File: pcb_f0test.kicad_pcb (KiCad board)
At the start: 2 copper layers, 50 x 50 mm, 93 parts, among them P1 CONN_02X05, P2 CONN_01X02, P3 CONN_01X06, P5 CONN_02X05, P6 CONN_02X05, P7 CONN_01X01, P8 CONN_01X01, U1 STM32F042GxU, U2 LP2985LV, U3 KNUSB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

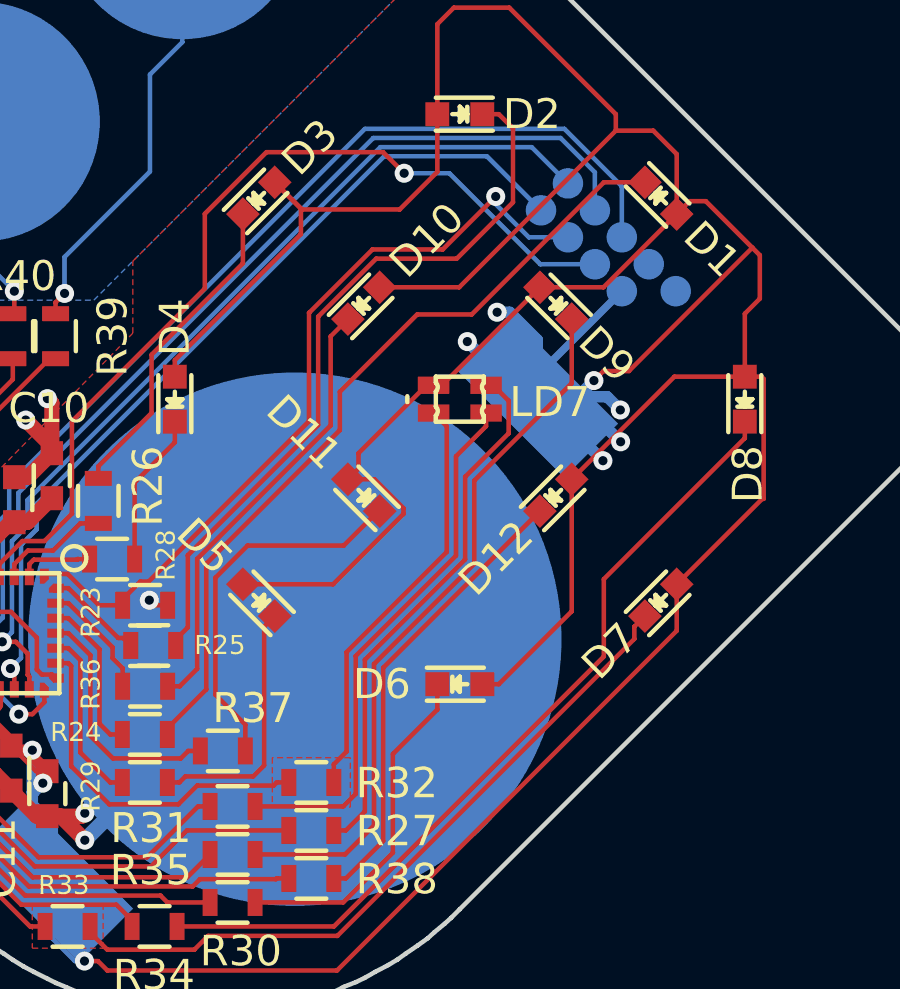
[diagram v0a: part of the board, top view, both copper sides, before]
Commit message: Switch RGB LED on heart PCB to new type/pinout.
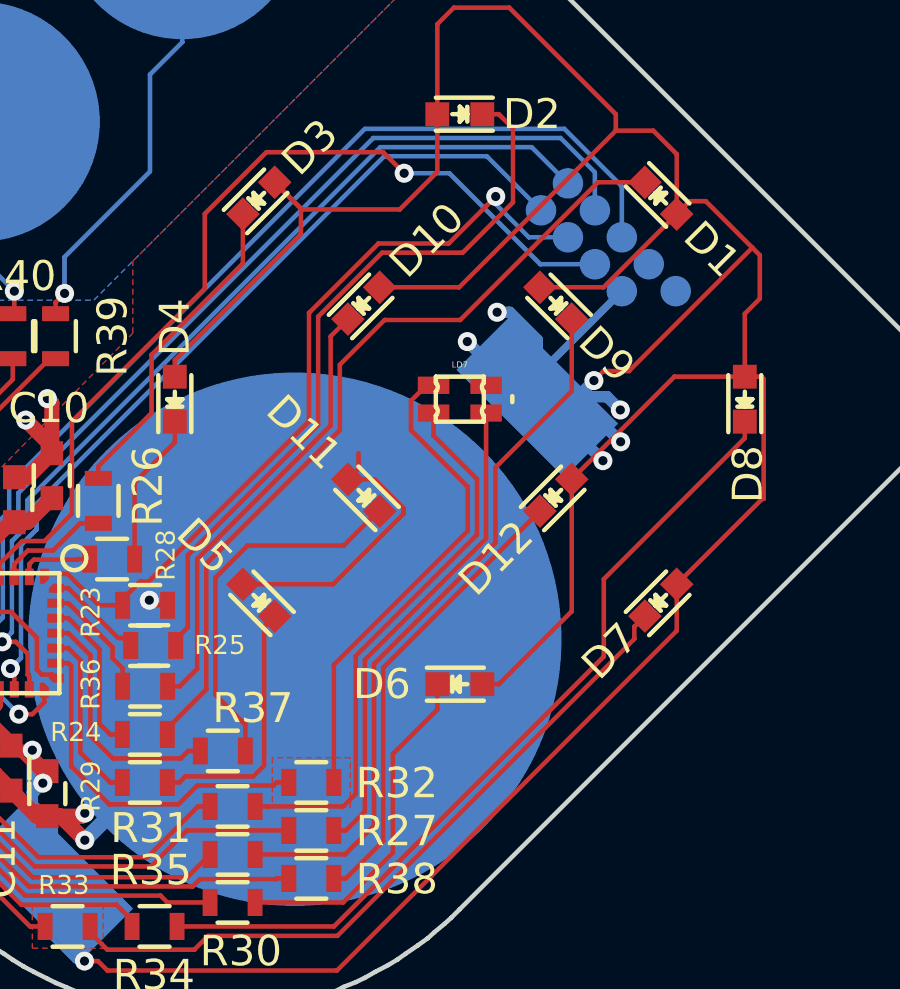
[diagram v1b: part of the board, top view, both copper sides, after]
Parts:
- LD7: footprint knielsenlib:RGB_0603 -> knielsenlib:RGB_0603_ALTPINOUT
- turned LD7 to 0 degrees
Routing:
- net +2V5: track 180.3 -> 172.0 mm
- net /sheet_heart/h_ildb1: track 14.1 -> 16.3 mm
- net /sheet_heart/h_ildr1: track 17.9 -> 16.3 mm
- net /sheet_heart/h_ild1: track 26.9 -> 27.4 mm

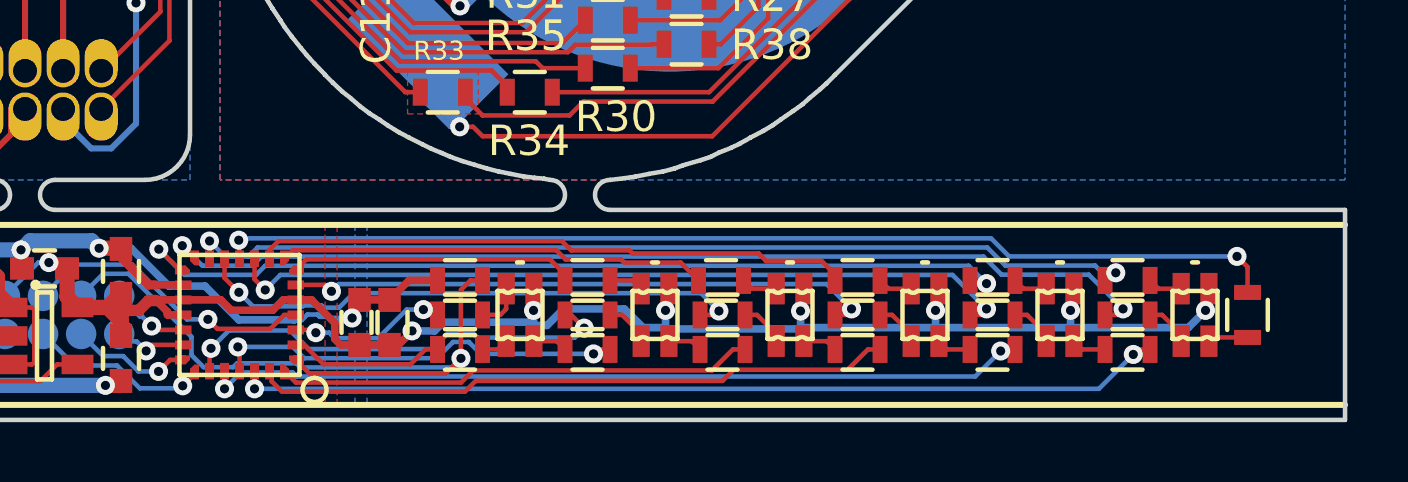
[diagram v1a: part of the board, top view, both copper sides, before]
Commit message: Change RGB LED footprint to match new batch of cheap 0603.
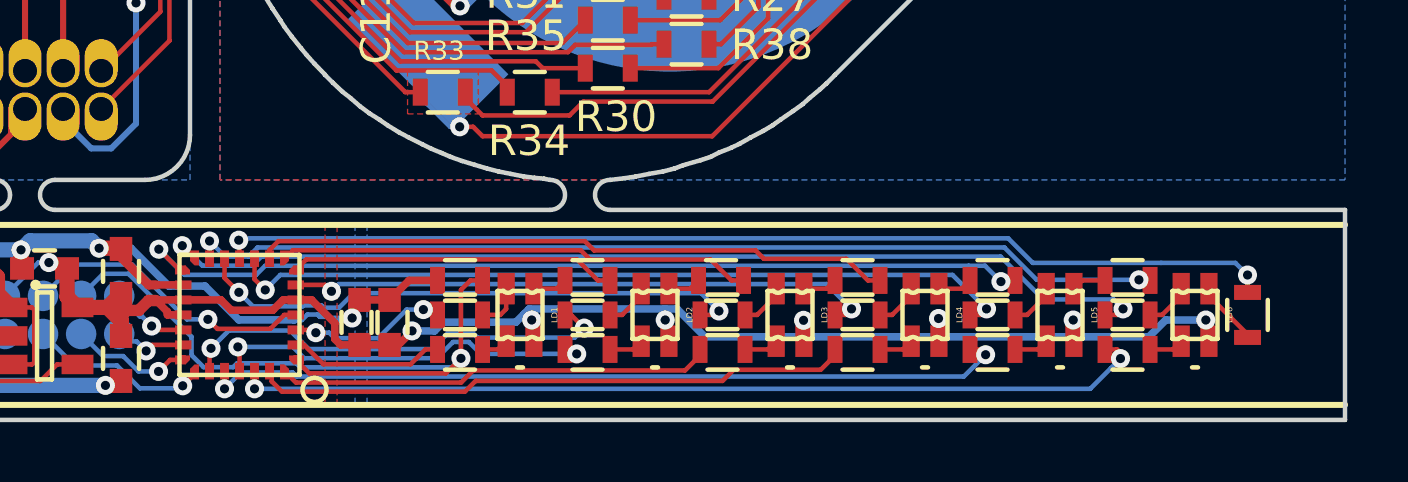
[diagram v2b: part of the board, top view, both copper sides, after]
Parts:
- LD1, LD2, LD3, LD4, LD5, LD6: footprint knielsenlib:RGB_0603 -> knielsenlib:RGB_0603_ALTPINOUT
- R2: value 560 -> 100
- R5: value 100 -> 560
- turned LD1 to 270 degrees
- turned LD2 to 270 degrees
- turned LD3 to 270 degrees
- turned LD4 to 270 degrees
- turned LD5 to 270 degrees
- turned LD6 to 270 degrees
- turned R12 to 180 degrees
- turned R13 to 180 degrees
- turned R14 to 0 degrees
- turned R15 to 0 degrees
- turned R18 to 180 degrees
- turned R19 to 180 degrees
- turned R3 to 0 degrees
- turned R6 to 180 degrees
- turned R8 to 0 degrees
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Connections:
- LD1 pad 2: /ildr2 -> /ildr1
- LD1 pad 3: /ildg2 -> /ildg1
- LD1 pad 4: /ildb2 -> /ildb1
- LD2 pad 2: /ildr3 -> /ildr2
- LD2 pad 3: /ildg3 -> /ildg2
- LD2 pad 4: /ildb3 -> /ildb2
- LD3 pad 2: /ildr4 -> /ildr3
- LD3 pad 3: /ildg4 -> /ildg3
- LD3 pad 4: /ildb4 -> /ildb3
- LD4 pad 2: /ildr5 -> /ildr4
- LD4 pad 3: /ildg5 -> /ildg4
- LD4 pad 4: /ildb5 -> /ildb4
- LD5 pad 2: /ildr6 -> /ildr5
- LD5 pad 3: /ildg6 -> /ildg5
- LD5 pad 4: /ildb6 -> /ildb5
- LD6 pad 2: /ildr1 -> /ildr6
- LD6 pad 3: /ildg1 -> /ildg6
- LD6 pad 4: /ildb1 -> /ildb6
- R10 pad 1: /ldg3 -> /ldg2
- R10 pad 2: /ildg3 -> /ildg2
- R11 pad 1: /ldg4 -> /ldg3
- R11 pad 2: /ildg4 -> /ildg3
- R12 pad 1: /ldb3 -> /ldb1
- R12 pad 2: /ildb3 -> /ildb1
- R13 pad 1: /ldb4 -> /ldb2
- R13 pad 2: /ildb4 -> /ildb2
- R16 pad 1: /ldg5 -> /ldg4
- R16 pad 2: /ildg5 -> /ildg4
- R17 pad 1: /ldg6 -> /ldg5
- R17 pad 2: /ildg6 -> /ildg5
- R18 pad 1: /ldb5 -> /ldb3
- R18 pad 2: /ildb5 -> /ildb3
- R19 pad 1: /ldb6 -> /ldb4
- R19 pad 2: /ildb6 -> /ildb4
- R2 pad 1: /ldr1 -> /ldb6
- R2 pad 2: /ildr1 -> /ildb6
- R4 pad 1: /ldg1 -> /ldg6
- R4 pad 2: /ildg1 -> /ildg6
- R5 pad 1: /ldg2 -> /ldr1
- R5 pad 2: /ildg2 -> /ildr1
- R6 pad 1: /ldb1 -> /ldb5
- R6 pad 2: /ildb1 -> /ildb5
- R7 pad 1: /ldb2 -> /ldg1
- R7 pad 2: /ildb2 -> /ildg1
- U1 pad 10: /ldg6 -> /ldg5
- U1 pad 11: /ldr1 -> /ldb6
- U1 pad 12: /ldg4 -> /ldg3
- U1 pad 13: /ldb1 -> /ldb5
- U1 pad 14: /ldg1 -> /ldg6
- U1 pad 15: /ldb6 -> /ldb4
- U1 pad 2: /ldg2 -> /ldr1
- U1 pad 23: /ldg3 -> /ldg2
- U1 pad 3: /ldb2 -> /ldg1
- U1 pad 6: /ldg5 -> /ldg4
- U1 pad 7: /ldb3 -> /ldb1
- U1 pad 8: /ldb4 -> /ldb2
- U1 pad 9: /ldb5 -> /ldb3
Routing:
- net /ldr1: track 35.5 -> 5.20 mm, vias 2 -> 0
- net /ldg1: track 33.8 -> 5.37 mm
- net /ldb1: track 32.0 -> 10.9 mm, vias 2 -> 0
- net /ldb4: track 14.3 -> 30.4 mm, vias 0 -> 2
- net /ldb5: track 19.9 -> 32.7 mm, vias 0 -> 2
- net /ldb3: track 9.53 -> 21.3 mm
- net /ldb2: track 5.37 -> 15.8 mm, vias 2 -> 0
- net /ldg2: track 5.20 -> 15.0 mm, vias 0 -> 2
- net /ldg6: track 26.5 -> 33.8 mm
- net /ldg5: track 19.7 -> 26.5 mm
- net /ldb6: track 30.2 -> 35.4 mm
- net /ldg3: track 15.0 -> 18.7 mm
- net /ldr3: track 16.0 -> 14.6 mm
- net /ldr4: track 21.4 -> 20.0 mm
- net /ildb6: track 1.15 -> 2.16 mm
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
